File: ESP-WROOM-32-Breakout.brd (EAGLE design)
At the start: 34.5 x 40 mm, 11 parts, among them Q1 2N7002, SW1 PROG, SW2 RST, U3 ESP-WROOM-32

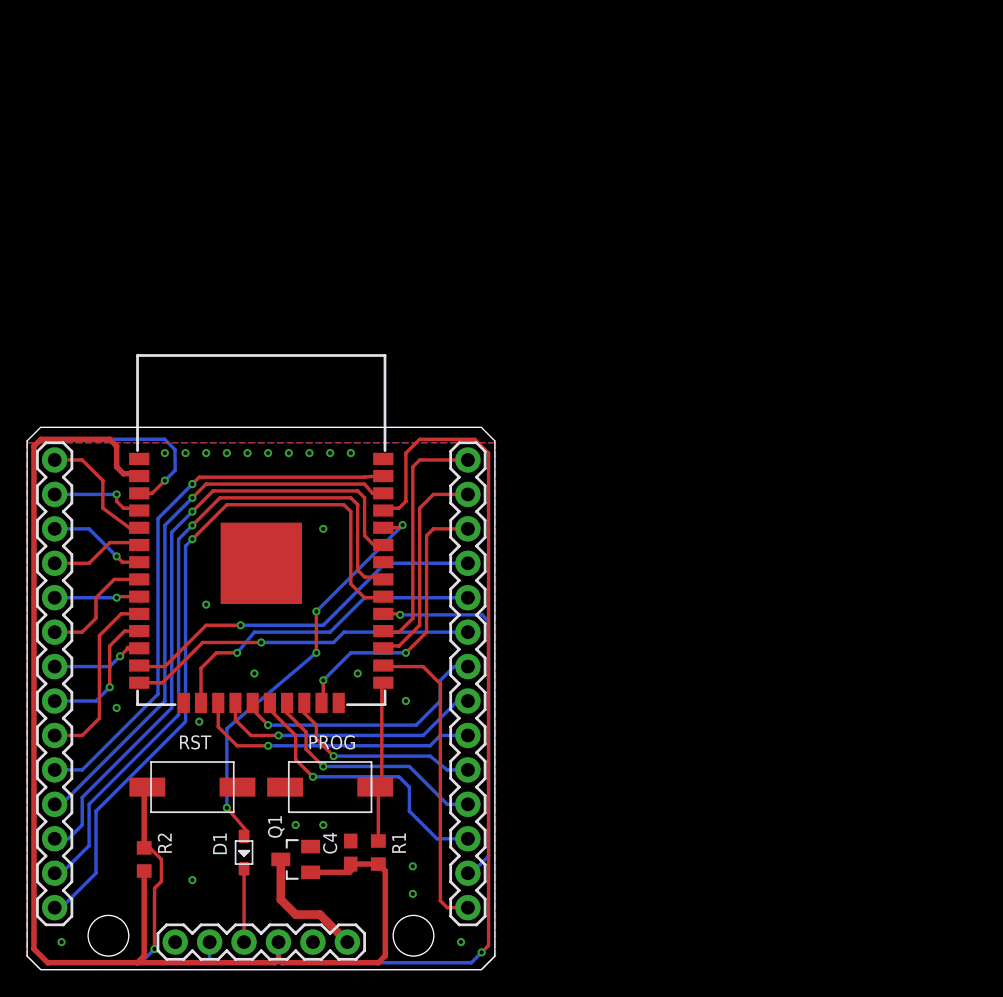
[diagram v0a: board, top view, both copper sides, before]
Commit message: Updated layout, added 3,3V regulators
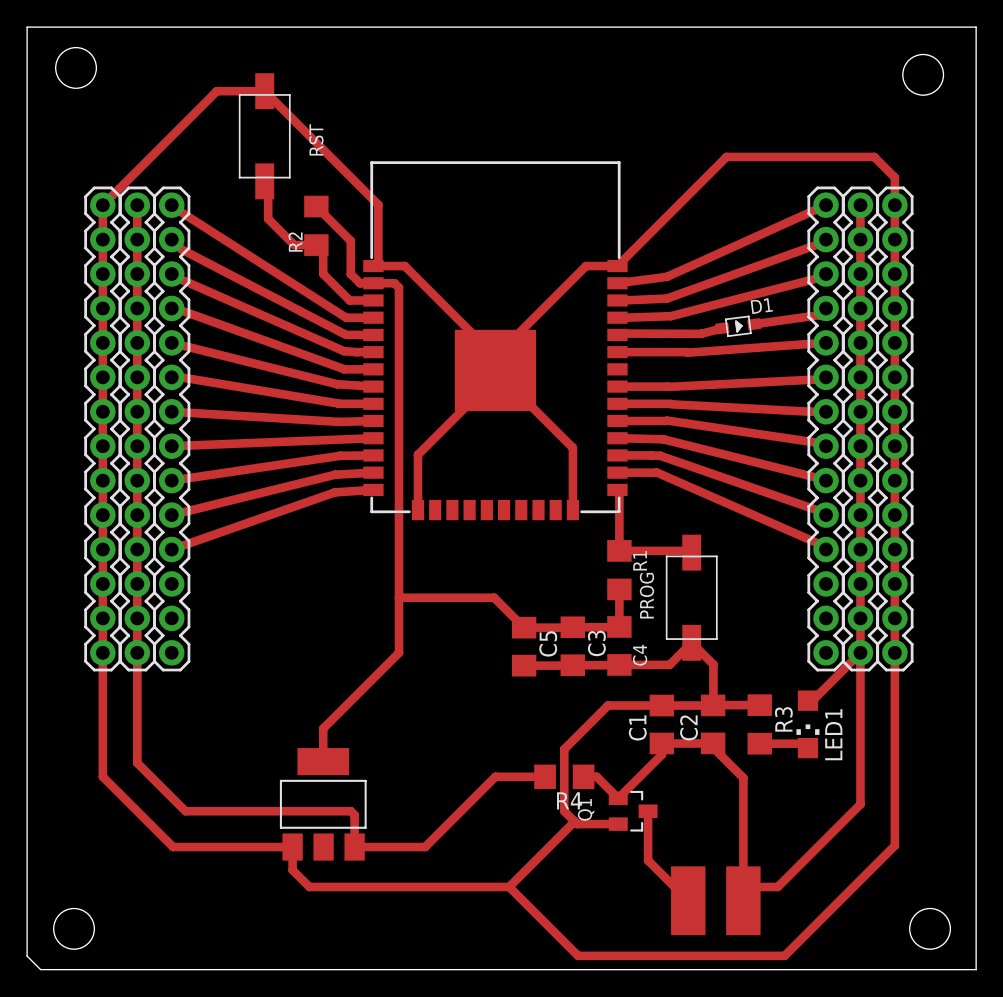
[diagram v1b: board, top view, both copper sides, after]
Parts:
- removed JP3: (no value), SparkFun-Connectors:1X06
- added C1, C3: 10uF, adafruit:C1206
- added C2, C5: 0.1uF, adafruit:C1206
- added IC1: REG1117, burr-brown:SOT223
- added JP4, JP5, JP6, JP7: (no value), SparkFun-Connectors:1X14
- added LED1: (no value), adafruit:CHIPLED_1206
- added PAD1, PAD2: (no value), wirepad:SMD2,54-5,08
- added R3: 330, adafruit:R1206
- added R4: 0, adafruit:R1206
- C4: device rcl:C0603 -> adafruit:C1206
- R1, R2: device rcl:R0603 -> adafruit:R1206
- moved D1 53.3 mm to (52.5, 47.5), turned to 7.3 degrees
- moved R2 48.4 mm to (21.3, 54.9), turned to 90 degrees
- moved SW2 48.3 mm to (17.5, 61.5), turned to 270 degrees
- moved JP2 32.4 mm to (58.9, 23.4)
- moved SW1 30.1 mm to (49.0, 27.4), turned to 90 degrees
- moved R1 27.4 mm to (43.7, 29.5)
- moved Q1 25.1 mm to (44.7, 11.7), turned to 270 degrees
- moved C4 25.0 mm to (43.7, 23.9), turned to 270 degrees
- moved U3 22.4 mm to (34.5, 44.2)
- moved JP1 20.7 mm to (10.7, 23.4)
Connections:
- new net 5V: C1.1, C2.1, IC1.3, JP4.1, JP4.10, JP4.11, JP4.12, JP4.13, JP4.14, JP4.2, JP4.3, JP4.4, JP4.5, JP4.6, JP4.7, JP4.8, JP4.9, JP5.1, JP5.10, JP5.11, JP5.12, JP5.13, JP5.14, JP5.2, JP5.3, JP5.4, JP5.5, JP5.6, JP5.7, JP5.8, JP5.9, LED1.A, PAD2.1, Q1.1, R4.1, R4.2
- new net N$1: LED1.C, R3.2
- net GND: now also C1.2, C2.2, C3.2, C5.2, IC1.1, JP6.1, JP6.10, JP6.11, JP6.12, JP6.13, JP6.14, JP6.2, JP6.3, JP6.4, JP6.5, JP6.6, JP6.7, JP6.8, JP6.9, JP7.1, JP7.10, JP7.11, JP7.12, JP7.13, JP7.14, JP7.2, JP7.3, JP7.4, JP7.5, JP7.6, JP7.7, JP7.8, JP7.9, R3.1
- net GND_IN: now also PAD1.1; no longer JP3.6
- net IO10: no longer JP2.7
- net IO11: no longer JP2.8
- net IO12: now also JP1.4; no longer JP2.9
- net IO13: no longer JP2.10
- net IO14: now also JP1.5; no longer JP2.11
- net IO15: no longer JP2.12
- net IO16: now also JP2.5; no longer JP2.13
- net IO17: now also JP2.6; no longer JP2.14
- net IO18: now also JP2.8; no longer JP1.1
- net IO19: now also JP2.9; no longer JP1.2
- net IO21: now also JP2.10; no longer JP1.3
- net IO22: now also JP2.13; no longer JP1.4
- net IO23: now also JP2.14; no longer JP1.5
- net IO25: now also JP1.8; no longer JP1.6
- net IO27: now also JP1.6; no longer JP1.8
- net IO32: now also JP1.10; no longer JP1.9
- net IO33: now also JP1.9; no longer JP1.10
- net IO34: now also JP1.12; no longer JP1.11
- net IO35: now also JP1.11; no longer JP1.12
- net IO36: now also JP1.14; no longer JP1.13
- net IO39: now also JP1.13; no longer JP1.14
- net IO4: now also JP2.4; no longer JP2.1
- net IO5: now also JP2.7; no longer JP2.2
- net IO6: no longer JP2.3
- net IO7: no longer JP2.4
- net IO8: no longer JP2.5
- net IO9: no longer JP2.6
- net RX: now also JP2.11; no longer JP3.3
- net TXD0: now also JP2.12; no longer JP3.2
- net VCC: now also C3.1, C5.1, IC1.2; no longer JP3.4, Q1.1
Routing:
- net GND: track 0.00 -> 318.4 mm, vias 24 -> 0
- net 5V: track 0.00 -> 163.0 mm
- net EN: track 76.4 -> 14.1 mm, vias 2 -> 0
- net TXD0: track 71.2 -> 15.8 mm, vias 1 -> 0
- net IO18: track 52.8 -> 15.4 mm, vias 1 -> 0
- net IO19: track 50.4 -> 15.5 mm, vias 1 -> 0
- net IO21: track 47.2 -> 15.5 mm, vias 1 -> 0
- net VCC: track 94.8 -> 66.7 mm
- net IO22: track 41.9 -> 16.2 mm, vias 1 -> 0
- net IO13: track 24.5 -> 0.00 mm, vias 1 -> 0
- net IO23: track 40.8 -> 16.6 mm, vias 1 -> 0
- net RXD0: track 30.8 -> 7.82 mm, vias 4 -> 0
- net IO15: track 21.2 -> 0.00 mm, vias 2 -> 0
- net IO6: track 21.1 -> 0.00 mm, vias 1 -> 0
- net IO9: track 21.1 -> 0.00 mm, vias 1 -> 0
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- removed copper zone on layer 1, net GND
- removed copper zone on layer 16, net GND
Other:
- board size 34.5 x 40 mm -> 70 x 69.5 mm
- board text added: "5V-in"
- board text removed: "12"
- board text removed: "14"
- board text removed: "15"
- board text removed: "17"
- board text removed: "By Studio Sophisti"
- board text removed: "ESP-WROOM-32 Breakout"
- board text removed: "V+"
